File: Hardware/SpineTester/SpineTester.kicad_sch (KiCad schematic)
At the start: 0 parts

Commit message: initial pcb commit
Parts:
- added P1: USB_C_Plug_USB2.0, Connector_USB:USB_C_Receptacle_JAE_DX07S016JA1R1500, symbol Connector:USB_C_Plug_USB2.0
- added U1: RP2040, Package_DFN_QFN:QFN-56-1EP_7x7mm_P0.4mm_EP3.2x3.2mm, symbol MCU_RaspberryPi:RP2040
- added U2, U3: HX711, Package_SO:SOP-16_3.9x9.9mm_P1.27mm, symbol Analog_ADC:HX711
- added U4: CH340C, Package_SO:SOIC-16_3.9x9.9mm_P1.27mm, symbol Interface_USB:CH340C
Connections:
- new net: P1.A1 (GND), P1.A12 (GND), P1.B1 (GND), P1.B12 (GND)
- new net: P1.A4 (VBUS), P1.A9 (VBUS), P1.B4 (VBUS), P1.B9 (VBUS)
- new net: P1.A6 (D+), U4.5 (UD+)
- new net: P1.A7 (D-), U4.6 (UD-)
- new net: U1.1 (IOVDD), U1.10 (IOVDD), U1.22 (IOVDD), U1.33 (IOVDD), U1.42 (IOVDD), U1.49 (IOVDD)
- new net: U1.23 (DVDD), U1.50 (DVDD)
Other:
- added sheet MCU (MCU.kicad_sch)
- added sheet WeightSense (WeightSense.kicad_sch)

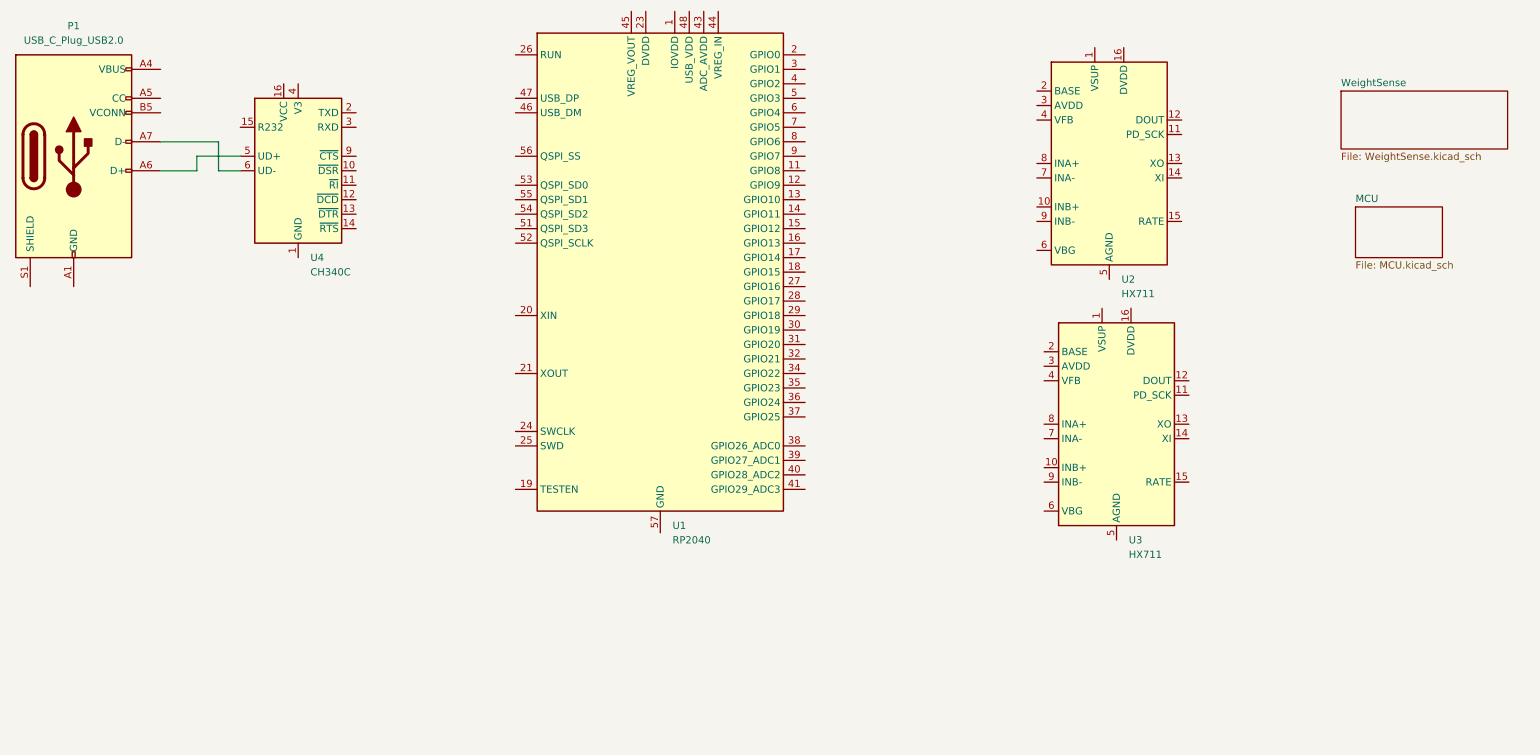
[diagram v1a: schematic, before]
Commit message: added connectors
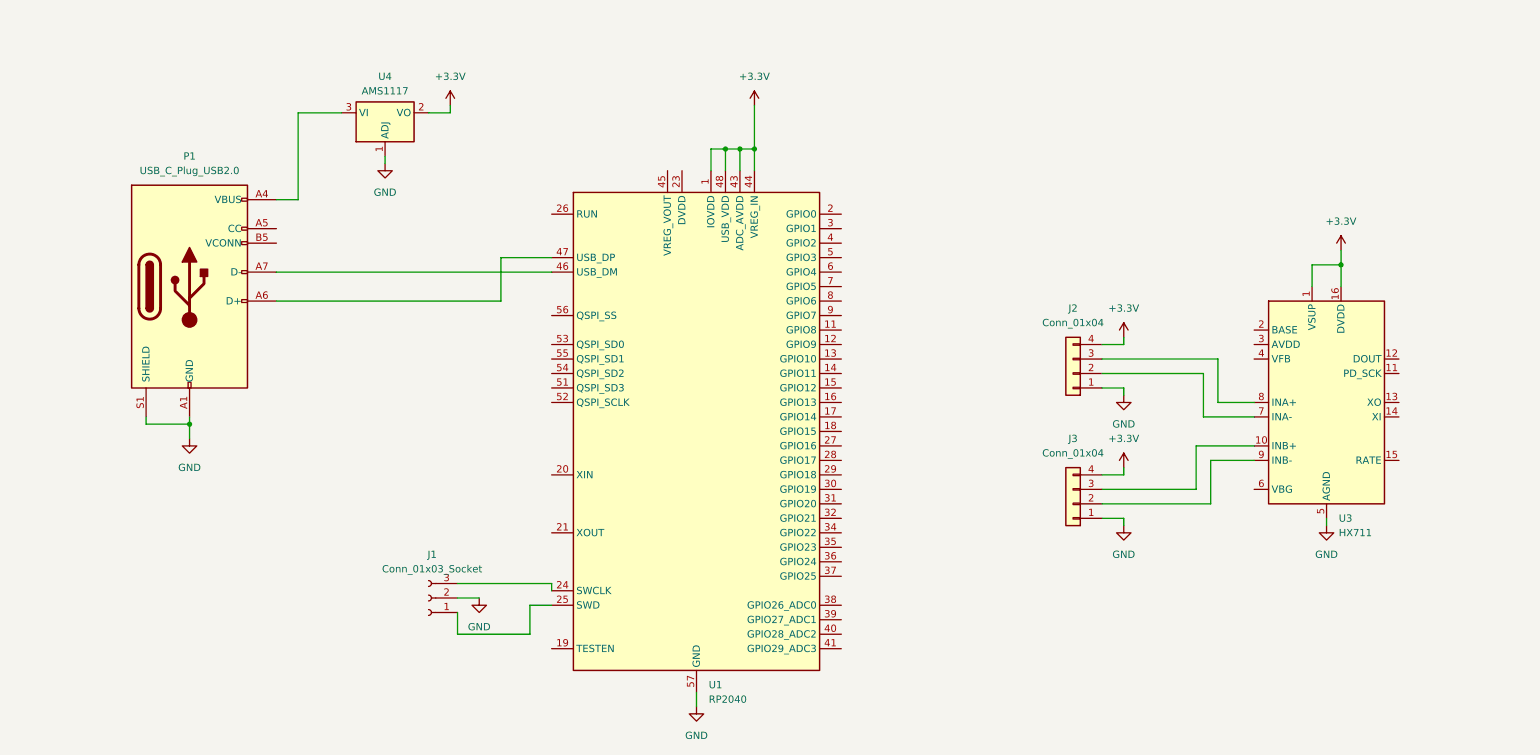
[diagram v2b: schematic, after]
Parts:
- removed U2: HX711, Package_SO:SOP-16_3.9x9.9mm_P1.27mm, symbol Analog_ADC:HX711
- removed U4: CH340C, Package_SO:SOIC-16_3.9x9.9mm_P1.27mm, symbol Interface_USB:CH340C
- added J1: Conn_01x03_Socket, Connector_JST:JST_SH_BM03B-SRSS-TB_1x03-1MP_P1.00mm_Vertical, symbol Connector:Conn_01x03_Socket
- added J2, J3: Conn_01x04, Connector_JST:JST_XH_B4B-XH-AM_1x04_P2.50mm_Vertical, symbol Connector_Generic:Conn_01x04
- added U4: AMS1117, Package_TO_SOT_SMD:SOT-223-3_TabPin2, symbol Regulator_Linear:AMS1117
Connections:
- net +3.3V: now reaches U3.1 (VSUP)
- net +3.3V: now also U1.1 (IOVDD), U1.10 (IOVDD), U1.22 (IOVDD), U1.33 (IOVDD), U1.42 (IOVDD), U1.43 (ADC_AVDD), U1.44 (VREG_IN), U1.48 (USB_VDD), U1.49 (IOVDD), U3.16 (DVDD), J2.4 (Pin_4), J3.4 (Pin_4), U4.2 (VO)
- net at U3.10 (INB+): now also J3.3 (Pin_3)
- net GND: now reaches U3.5 (AGND)
- net GND: now also P1.A1 (GND), P1.A12 (GND), P1.B1 (GND), P1.B12 (GND), P1.S1 (SHIELD), U1.57 (GND), J1.2 (Pin_2), J2.1 (Pin_1), J3.1 (Pin_1), U4.1 (ADJ)
- net at U3.7 (INA-): now also J2.2 (Pin_2)
- net at U3.8 (INA+): now also J2.3 (Pin_3)
- net at U3.9 (INB-): now also J3.2 (Pin_2)
- net at P1.A4 (VBUS), P1.A9 (VBUS), P1.B4 (VBUS)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: now also U4.3 (VI)
- net at P1.A6 (D+): now also U1.47 (USB_DP)
- net at P1.A7 (D-): now also U1.46 (USB_DM)
- net at U1.24 (SWCLK): now also J1.3 (Pin_3)
- net at U1.25 (SWD): now also J1.1 (Pin_1)
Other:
- removed sheet MCU
- removed sheet WeightSense
- moved on the sheet: P1, U1

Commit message: changed connectors
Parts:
- J2, J3: footprint Connector_JST:JST_XH_B4B-XH-AM_1x04_P2.50mm_Vertical -> Library:Solderpad
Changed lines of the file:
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@@
 			)
 		)
-		(property "Footprint" "Connector_JST:JST_XH_B4B-XH-AM_1x04_P2.50mm_Vertical"
+		(property "Footprint" "Library:Solderpad"
 			(at 205.74 104.14 0)
 			(effects
@@
 			)
 		)
-		(property "Footprint" "Connector_JST:JST_XH_B4B-XH-AM_1x04_P2.50mm_Vertical"
+		(property "Footprint" "Library:Solderpad"
 			(at 205.74 81.28 0)
 			(effects
